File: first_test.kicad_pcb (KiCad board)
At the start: 2 copper layers, 64.5 x 13.5 mm, 11 parts, among them J1 USB-C, J3 Conn_01x04, U1 STM32F103C6Ux, U2 TDN_5-0910WISM, Y1 8Mhz

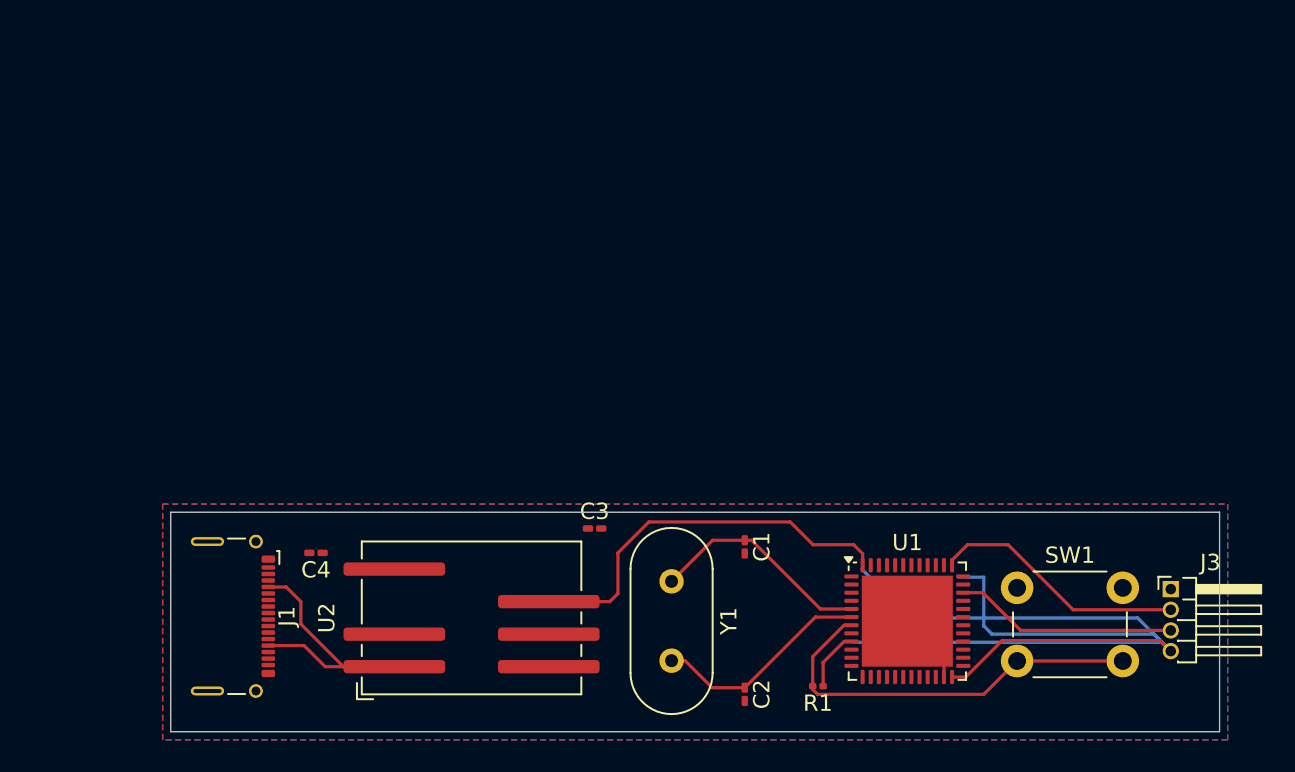
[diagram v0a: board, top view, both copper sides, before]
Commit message: feat: add customize symbol and footprint
Signed-off-by: briq <990647625@qq.com>
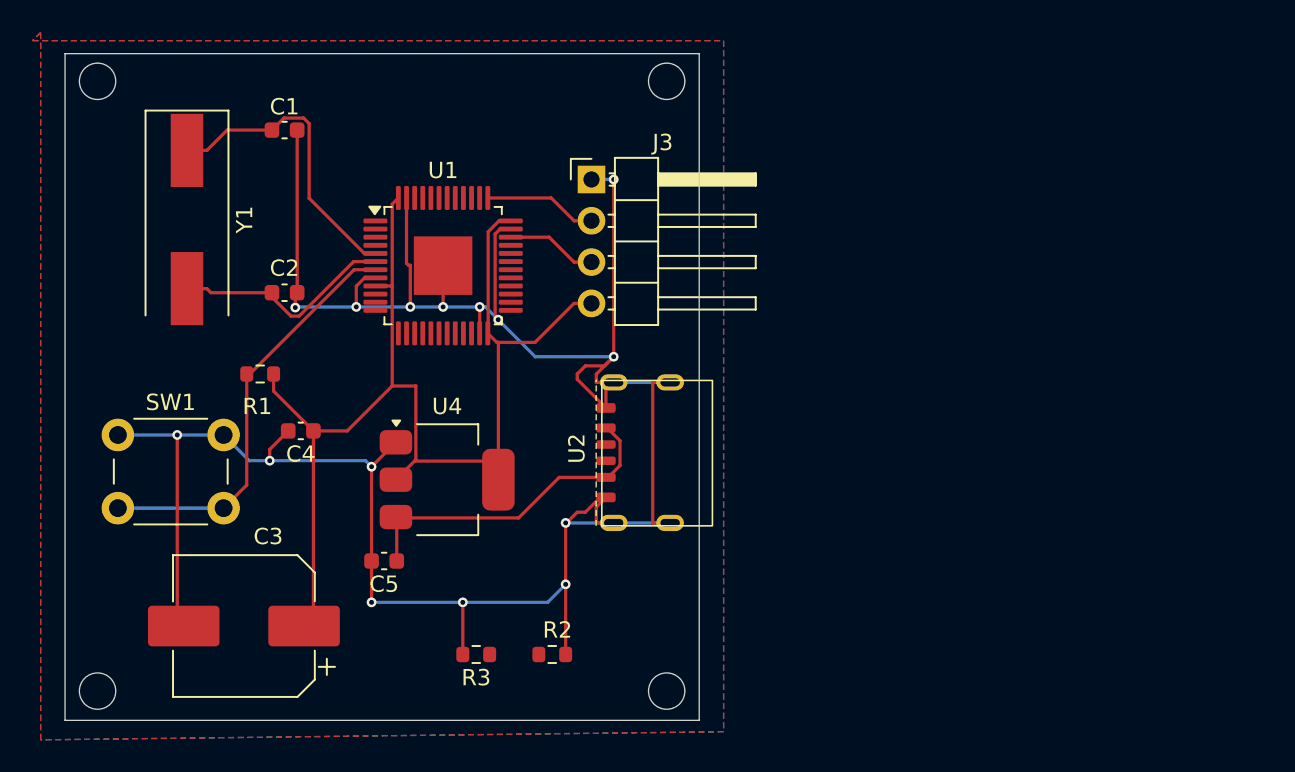
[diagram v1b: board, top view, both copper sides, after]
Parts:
- removed J1: USB-C, Connector_USB:USB_C_Receptacle_G-Switch_GT-USB-7025
- added C5: 10uf, Capacitor_SMD:C_0603_1608Metric, F.Cu at (110.1, 91.0)
- added R2: 10k, Resistor_SMD:R_0603_1608Metric, F.Cu at (120.5, 96.8)
- added R3: 10k, Resistor_SMD:R_0603_1608Metric, F.Cu at (115.8, 96.8)
- added U4: AMS1117-3.3, Package_TO_SOT_SMD:SOT-223-3_TabPin2, F.Cu at (114.0, 86.0)
- C1, C2: value 1.2pf -> 18pf; footprint Capacitor_SMD:C_0201_0603Metric_Pad0.64x0.40mm_HandSolder -> Capacitor_SMD:C_0603_1608Metric
- C3: value 1.2pf -> 100uf; footprint Capacitor_SMD:C_0201_0603Metric_Pad0.64x0.40mm_HandSolder -> Capacitor_SMD:CP_Elec_8x10.5
- C4: value 1.2pf -> 10uf; footprint Capacitor_SMD:C_0201_0603Metric_Pad0.64x0.40mm_HandSolder -> Capacitor_SMD:C_0603_1608Metric
- J3: footprint Connector_PinHeader_1.27mm:PinHeader_1x04_P1.27mm_Horizontal -> Connector_PinHeader_2.54mm:PinHeader_1x04_P2.54mm_Horizontal
- R1: value 2k -> 40k; footprint Resistor_SMD:R_0201_0603Metric -> Resistor_SMD:R_0603_1608Metric
- SW1: value ~ -> switch
- U1: footprint Package_DFN_QFN:QFN-48-1EP_7x7mm_P0.5mm_EP5.6x5.6mm -> Package_QFP:LQFP-48-1EP_7x7mm_P0.5mm_EP3.6x3.6mm
- U2: value TDN_5-0910WISM -> usb type-c; footprint Converter_DCDC:Converter_DCDC_TRACO_TDN_5-xxxxWISM_SMD -> first_test:usb_c_6pin
- Y1: footprint Crystal:Crystal_HC49-4H_Vertical -> Crystal:Crystal_SMD_HC49-SD
- moved SW1 56.1 mm to (93.8, 83.2)
- moved J3 43.6 mm to (122.9, 67.5)
- moved R1 39.3 mm to (102.5, 79.5)
- moved C1 38.2 mm to (104.0, 64.5), turned to 0 degrees
- moved C2 37.6 mm to (104.0, 74.5), turned to 0 degrees
- moved Y1 37.2 mm to (98.0, 70.0)
- moved U1 36.0 mm to (113.8, 72.8)
- moved C3 22.4 mm to (101.5, 95.0), turned to 180 degrees
- moved U2 13.4 mm to (124.2, 84.3)
- moved C4 7.56 mm to (105.0, 83.0)
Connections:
- C4 pad 1: Net-(U2-+VIN) -> +3.3V
- U2 pad 7: +3.3V -> GND
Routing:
- net GND: track 7.55 -> 165.9 mm, vias 0 -> 15
- net +3.3V: track 100.1 -> 72.3 mm
- net +5V: track 0.00 -> 20.5 mm
- net Net-(U2-+VIN): track 18.9 -> 0.00 mm
- net /swclk: track 15.8 -> 6.96 mm
- net /swdio: track 13.7 -> 5.60 mm
- net /osc_in: track 13.9 -> 18.6 mm
- net /NRST: track 25.2 -> 25.9 mm
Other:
- board size 64.5 x 13.5 mm -> 39 x 41 mm

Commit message: feat: add marker for smt
Signed-off-by: briq <990647625@qq.com>
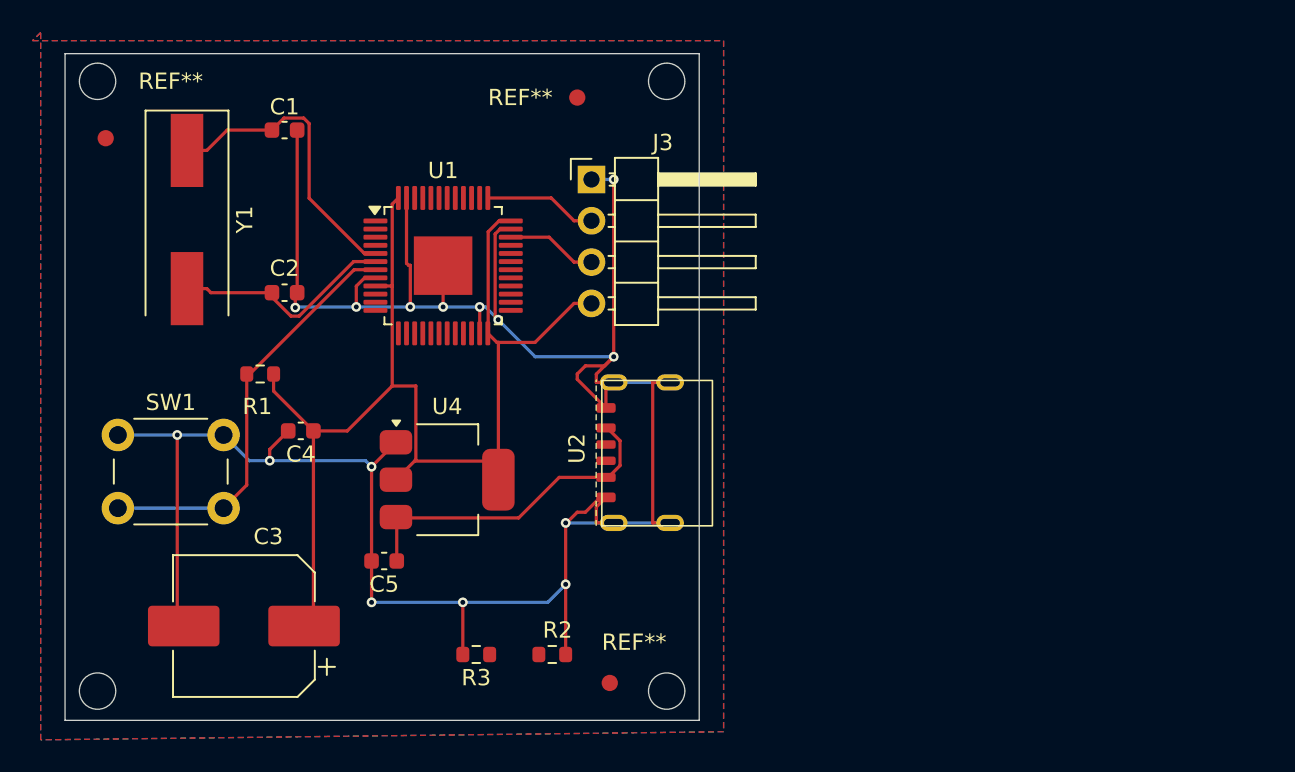
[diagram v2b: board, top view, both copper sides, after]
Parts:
- added REF**: Fiducial_1mm_Mask2mm, Fiducial:Fiducial_1mm_Mask2mm, F.Cu at (93.0, 65.0)
- added REF**: Fiducial_1mm_Mask2mm, Fiducial:Fiducial_1mm_Mask2mm, F.Cu at (122.0, 62.5)
- added REF**: Fiducial_1mm_Mask2mm, Fiducial:Fiducial_1mm_Mask2mm, F.Cu at (124.0, 98.5)
